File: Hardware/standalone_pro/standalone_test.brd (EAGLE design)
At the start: 110 x 100 mm, 104 parts, among them IC2 AP1212, IC3 AP1212, Q2 32.768khz, U1 NMOS_2N7002, U10 ZXCT1107SA-7, U2 DMS3016SSS-13, U3 DMS3016SSS-13, U5 NMOS_2N7002, U6 NMOS_2N7002, U7 INA213AIDCKT, U9 PMOS_RSS090P03, X1 KUSBVX, X2 KUSBVX, X3 KUSBVX, X4 KUSBVX

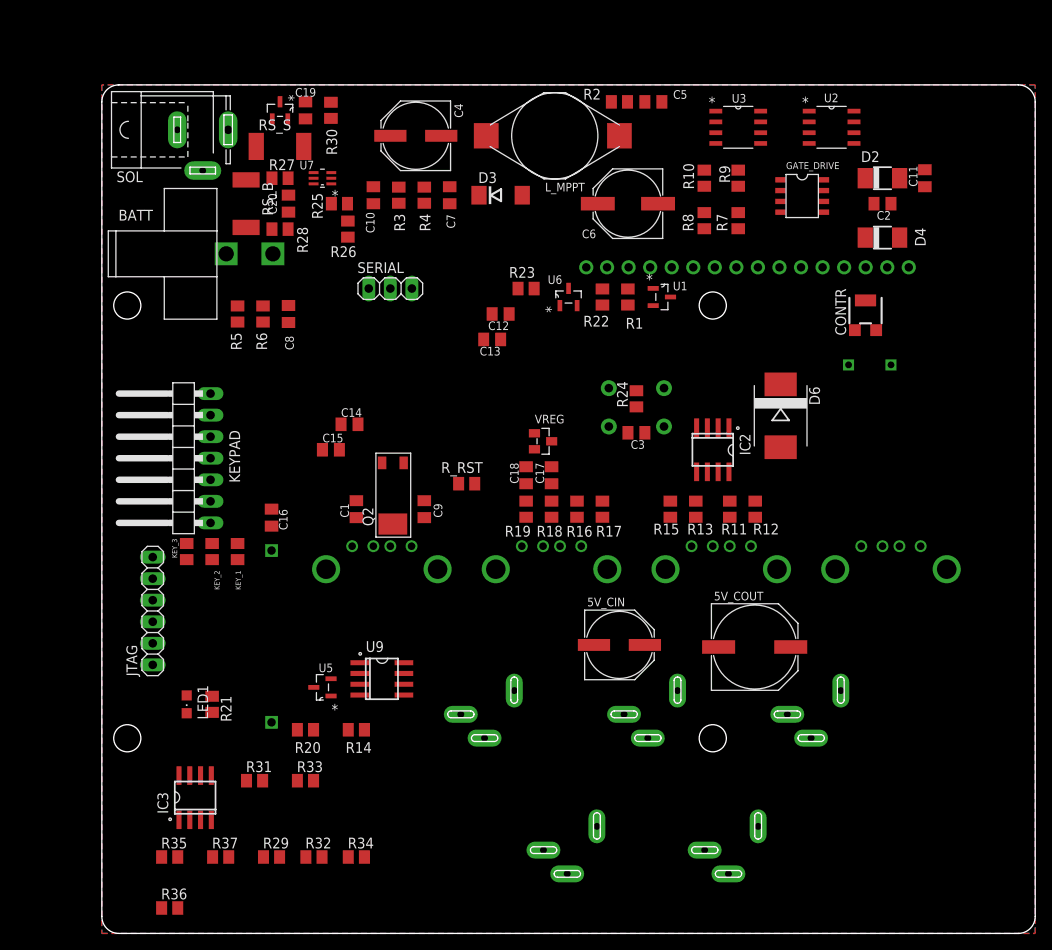
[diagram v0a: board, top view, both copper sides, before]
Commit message: Standalone pro physical layout finalised
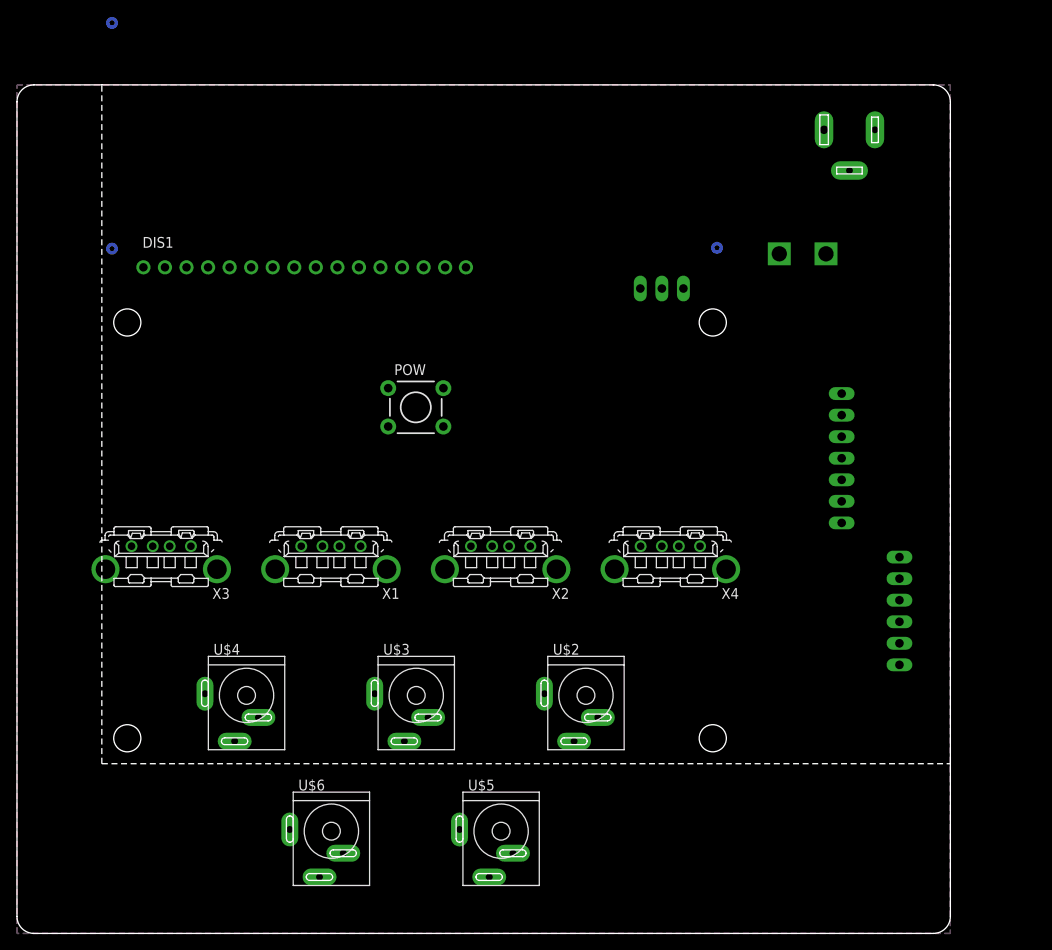
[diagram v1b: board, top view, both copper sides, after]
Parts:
- removed 5V_CIN: 100u, resistor:PANASONIC_E
- removed 5V_COUT: 1000uF, resistor:PANASONIC_G
- removed BATT_BCKUP: RENATA_COIN_CELL, coin_cells:PANASONIC_CR2032_1298246
- removed BUZZ1: BUZZ_14MM, buzzer:14MM_5M_PINS
- removed C1, C9: 12.5pF, resistor:C0805K
- removed C10, C11, C12, C16, C17, C18, C19, C2: 1uF, resistor:C0805K
- removed C13, C14, C15, C3: 100nF, resistor:C0805K
- removed C20, C7, C8: 10uF, resistor:C0805K
- removed C4: 100uF, resistor:PANASONIC_E
- removed C5: 0.1uF, resistor:C0805K
- removed C6: 220uF, resistor:PANASONIC_F
- removed CONTR: 10K, resistor:RTRIM3304W
- removed D2: S1A-E3/5AT, diode:DO-214AC
- removed D3: (no value), equinox:DO214AA
- removed D4: US1D - 1625280, diode:DO-214AC
- removed D6: B340-13-F, equinox:SMC
- removed GATE_DRIVE: IR2104S, equinox:IR2104S
- removed IC2, IC3: AP1212, equinox:SO8
- removed KEY_1, KEY_2, KEY_3, R25, R26, R3, R5: 10K, rcl:M0805
- removed LED1: POW_3V3, led:CHIPLED_0805
- removed L_MPPT: 330u, equinox:INDUC_BOURNS_SDR1806
- removed Q2: 32.768khz, equinox:CRYSTAL_CMJ206T
- removed R1, R23, R24: 1k, resistor:M0805
- removed R10, R9: 5, rcl:M0805
- removed R11, R13, R16, R18, R29, R32, R34, R36: 75k, resistor:M0805
- removed R12, R15, R17, R19, R31, R33, R35, R37: 49.9k, resistor:M0805
- removed R14, R_RST: 100K, rcl:M0805
- removed R2, R7, R8: 200, rcl:M0805
- removed R20: 1k, rcl:M0805
- removed R21: 1K, resistor:M0805
- removed R22: 0R, resistor:M0805
- removed R27, R28: 10, rcl:M0805
- removed R30: 1k65, rcl:M0805
- removed R4, R6: 1.32k, rcl:M0805
- removed RS_B: 0.01, rcl:R2512
- removed RS_S: 0.1, rcl:R2512
- removed U1, U5, U6: NMOS_2N7002, equinox:SOT103P240X110-3N
- removed U10: ZXCT1107SA-7, equinox:SOT91P240X110-3N
- removed U2, U3: DMS3016SSS-13, equinox:SOIC127P600X175-8N
- removed U7: INA213AIDCKT, equinox:SOT65P210X110-6N
- removed U9: PMOS_RSS090P03, equinox:SO8
- removed VREG: MCP1700T-3302E/TT, equinox:SOT95P237X112-3N
- moved DIS1 106.2 mm to (-3.10, 56.0), flipped to the top
- moved JTAG 88.0 mm to (94.0, 18.0), flipped to the bottom
- moved X3 86.0 mm to (7.00, 25.6), flipped to the top
- moved KEYPAD 82.0 mm to (91.0, 36.0), flipped to the bottom
- moved SOL 76.2 mm to (88.1, 74.7), flipped to the bottom
- moved BATT 70.7 mm to (85.3, 60.1), flipped to the bottom
- moved U$4 65.2 mm to (17.0, 8.00), flipped to the top
- moved X1 46.0 mm to (27.0, 25.6), flipped to the top
- moved U$6 45.5 mm to (27.0, -8.00), flipped to the top
- moved X4 34.0 mm to (67.0, 25.6), flipped to the top
- moved SERIAL 32.0 mm to (66.0, 56.0), flipped to the bottom
- moved U$3 26.0 mm to (37.0, 8.00), flipped to the top
- moved POW 26.0 mm to (37.0, 42.0), flipped to the top
- moved U$1 23.4 mm to (38.3, 35.9), flipped to the top
- moved U$2 13.2 mm to (57.0, 8.00), flipped to the top
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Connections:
- removed net +3V3: C12.2, C13.2, C14.2, C15.2, C18.2, JTAG.1, KEY_1.2, KEY_2.2, KEY_3.2, LED1.A, POW.3, POW.4, R25.2, R_RST.2, U7.3, VREG.2
- removed net 12V_OUT: U$2.1, U$3.1, U$4.1, U9.5, U9.6, U9.7, U9.8
- removed net 12V_OUT1: U$5.1, U$6.1
- removed net 12V_OUT_EN: R20.1
- removed net BATT_I: U7.6
- removed net BATT_V: C8.2, R5.1, R6.2
- removed net CC_EN: R8.1
- removed net CC_PWM: R7.1
- removed net LCD_BK_EN: R23.1
- removed net LCD_PWR: R1.2
- removed net N$1: C1.2, Q2.P$2
- removed net N$10: C2.1, D2.C, GATE_DRIVE.8
- removed net N$11: R10.1, U3.4
- removed net N$12: C6.+, D3.A, L_MPPT.P$2, R2.1
- removed net N$13: GATE_DRIVE.5, R10.2
- removed net N$14: R9.1, U2.4
- removed net N$15: C5.2, R2.2
- removed net N$16: C10.1, C11.2, C4.+, D2.A, GATE_DRIVE.1, R3.2, RS_S.2, U10.2, U2.5, U2.6, U2.7, U2.8
- removed net N$17: R1.1, U1.1
- removed net N$18: C9.2, Q2.P$3
- removed net N$21: D6.C
- removed net N$22: BUZZ1.P$1
- removed net N$25: R14.1, U5.3, U9.4
- removed net N$3: GATE_DRIVE.3, R8.2
- removed net N$32: R23.2, U6.1
- removed net N$35: R20.2, U5.1
- removed net N$37: LED1.C, R21.2
- removed net N$39: R25.1, R26.2, U7.1
- removed net N$40: C20.2, R27.1, U7.4
- removed net N$41: C20.1, R28.1, U7.5
- removed net N$43: R32.1, R33.2, X3.3
- removed net N$44: R34.1, R35.2, X4.2
- removed net N$45: R36.1, R37.2, X4.3
- removed net N$6: C2.2, C5.1, D4.C, GATE_DRIVE.6, L_MPPT.P$1, U2.1, U2.2, U2.3, U3.5, U3.6, U3.7, U3.8
- removed net N$7: GATE_DRIVE.7, R9.2
- removed net N$8: GATE_DRIVE.2, R7.2
- removed net NRST: JTAG.5, R_RST.1
- removed net SOL_I: C19.2, R30.2, U10.1
- removed net SOL_V: C7.2, R3.1, R4.2
- removed net USB_EN1: IC2.1, IC3.1
- removed net USB_EN2: IC2.4, IC3.4
- removed net USB_FLG1: IC2.2, IC3.2
- removed net USB_FLG2: IC2.3, IC3.3
- removed net USB_OUT1: IC2.8, IC3.8, R11.2, R13.2, R29.2, R32.2, X1.1, X3.1
- removed net USB_OUT2: IC2.5, IC3.5, R16.2, R18.2, R34.2, R36.2, X2.1, X4.1
- removed net V_BACKUP: BATT_BCKUP.P+, C16.2
- removed net V_LOAD: 5V_CIN.+, D3.C, R14.2, R27.2, R5.2, RS_B.1, U9.1, U9.2, U9.3
- new net S$1: JTAG.1
- new net S$6: POW.3, POW.4
- new net S$7: U$2.2, U$2.3
- net +5V: no longer 5V_COUT.+, C17.2, CONTR.3, IC2.7, IC3.7, R22.2, VREG.3
- net GND: no longer 5V_CIN.-, 5V_COUT.-, BATT_BCKUP.P-, BUZZ1.P$2, C1.1, C10.2, C11.1, C12.1, C13.1, C14.1, C15.1, C16.1, C17.1, C18.1, C19.1, C3.1, C4.-, C6.-, C7.1, C8.1, C9.1, D4.A, D6.A, GATE_DRIVE.4, IC2.6, IC3.6, JTAG.3, Q2.CASE, R12.1, R15.1, R17.1, R19.1, R21.1, R24.2, R26.1, R30.1, R31.1, R33.1, R35.1, R37.1, R4.1, R6.1, U1.2, U3.1, U3.2, U3.3, U5.2, U6.2, U7.2, VREG.1
- net N$19: no longer R22.1
- net N$2: no longer CONTR.2
- net N$20: no longer R16.1, R17.2
- net N$23: no longer KEY_1.1
- net N$24: no longer KEY_2.1
- net N$26: no longer KEY_3.1
- net N$31: no longer U6.3
- net N$33: no longer R11.1, R12.2
- net N$34: no longer R13.1, R15.2
- net N$36: no longer R18.1, R19.2
- net N$38: no longer RS_S.1, U10.3
- net N$4: no longer R28.2, RS_B.2
- net N$42: no longer R29.1, R31.2
- net N$46: no longer U$2.2, U$2.3, U$4.3
- net N$5: no longer CONTR.1, DIS1.1, U1.3
- net WKUP: no longer C3.2, POW.1, R24.1
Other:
- outline, holes or cut-outs redrawn
